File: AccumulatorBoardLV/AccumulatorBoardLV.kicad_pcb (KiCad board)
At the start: 4 copper layers, 152.4 x 50.8 mm, 50 parts, among them J1 Contactor 1, J10 To HV Board, J11 IMD Reset, J12 TS Interlock, J13 Temp Reset, J14 To ECU, J15 Charger LV, J16 Charger Interlock, J17 Lid Interlock, J18 From HV Board, J19 Chip 1, J2 BMS Connector 1, J20 Chip 2, J21 Chip 3, J22 Chip 4, J3 BMS Connector 2, J4 BMS TX, J5 BMS RX, J6 Current Sensor, J7 Contactor 2, J8 IMD LV, J9 BMS Reset, U1 DE1A1B-L2-12V, U10 MCP3008, U11 ISO1050, U12 stm_nucleo_FK303K8, U13 MCP3008, U14 MCP3008, U2 LM555N, U3 SN754410, U4 DE1A1B-L2-12V, U5 L78S05CV-DG, U6 DE1A1B-L2-12V, U7 DK1A1B-12V, U8 ADUM4154ARIZ, U9 MCP3008

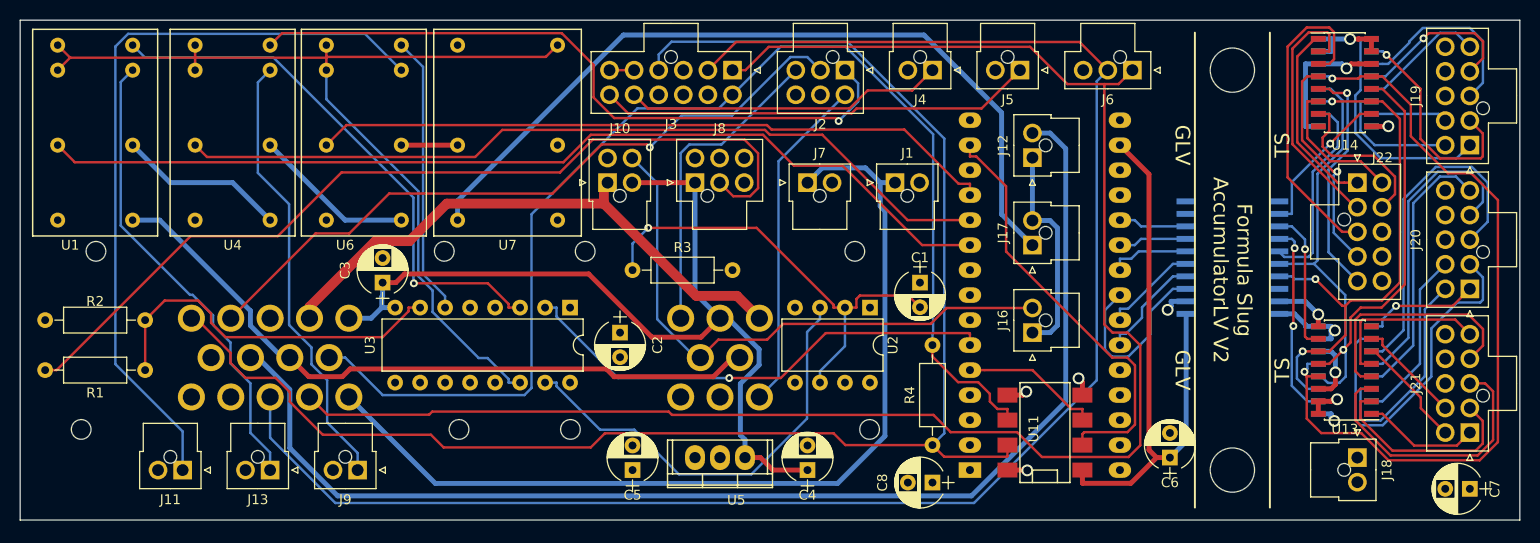
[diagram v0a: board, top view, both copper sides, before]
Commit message: update some footprint throughole sizes
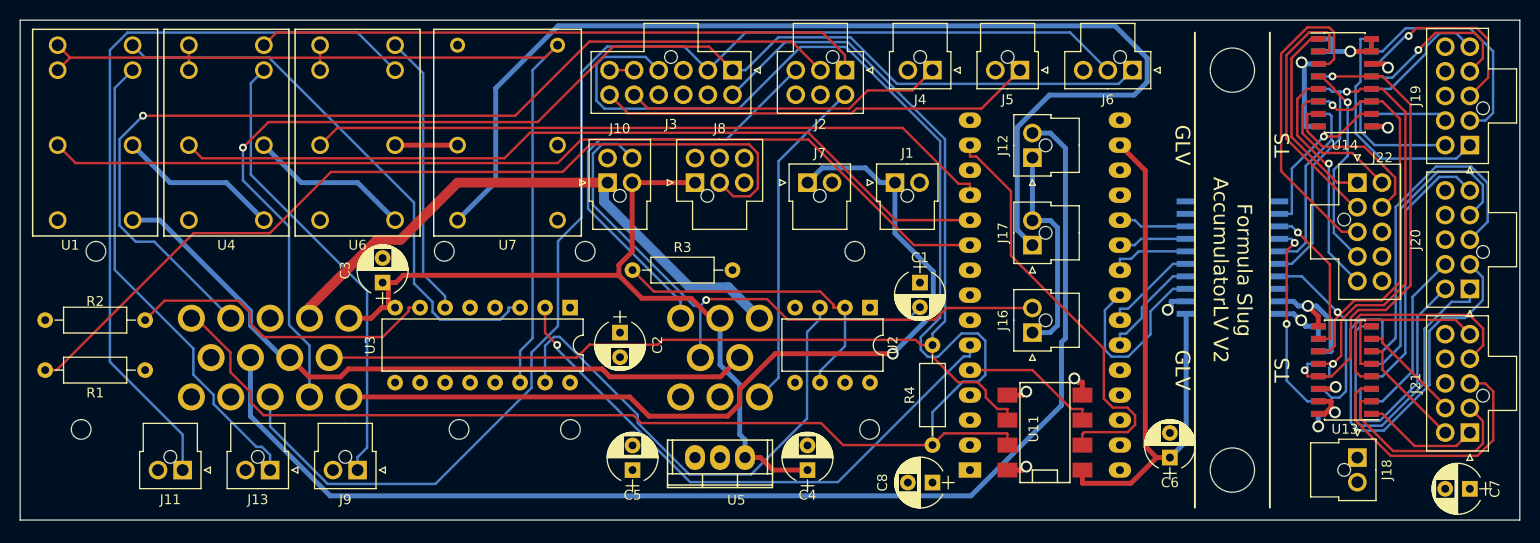
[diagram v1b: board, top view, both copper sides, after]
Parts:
- moved U4 0.63 mm to (57.4, 119.9)
- moved U6 0.63 mm to (70.7, 119.9)
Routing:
- net /5V_BMS: track 170.6 -> 127.7 mm, vias 0 -> 1
- net /SIG_CURRENT: track 171.1 -> 128.9 mm
- net /AIRS_RELAYS_OUT: track 82.3 -> 115.3 mm
- net /SCLK: track 80.1 -> 48.2 mm
- net /CAN_H: track 159.1 -> 188.3 mm
- net /V_L: track 71.7 -> 100.5 mm
- net Net-(J20-Pad1): track 12.0 -> 32.5 mm, vias 1 -> 0
- net /3.3V_TS: track 21.4 -> 35.4 mm
- net /V_S: track 32.0 -> 45.4 mm
- net /TEMP_SSO: track 76.2 -> 65.3 mm, vias 1 -> 2
- net /BATT-: track 31.2 -> 41.6 mm, vias 5 -> 6
- net /TEMP_FLT: track 49.7 -> 58.7 mm
- net +12V: track 91.2 -> 82.5 mm
- net /BMS_FLT: track 70.5 -> 62.1 mm, vias 1 -> 0
- net Net-(J20-Pad2): track 35.1 -> 42.7 mm
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
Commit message: update Arduino (used for STMF3) footprint as well
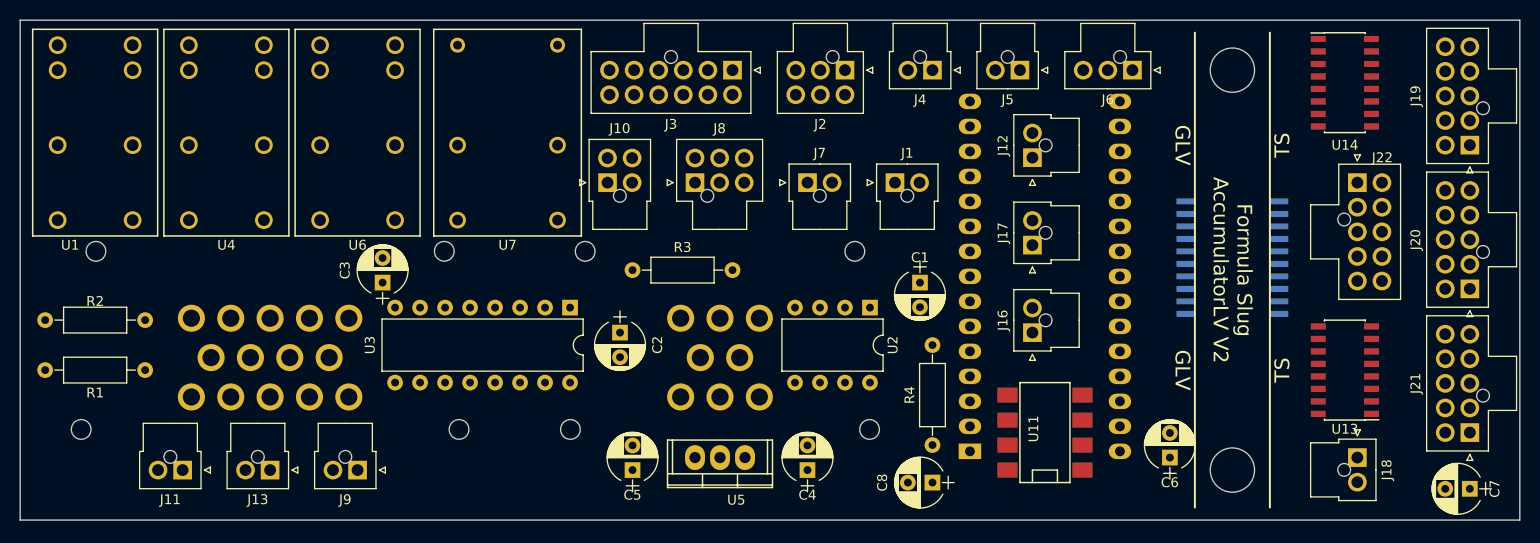
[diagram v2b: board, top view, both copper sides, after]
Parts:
- moved U12 1.91 mm to (144.4, 132.0)
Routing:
- net /CAN_H: track 188.3 -> 0.00 mm
- net /SIG_CURRENT: track 128.9 -> 0.00 mm
- net /5V_BMS: track 127.7 -> 0.00 mm, vias 1 -> 0
- net /AIRS_ACC_OUT: track 125.8 -> 0.00 mm
- net /CAN_L: track 124.2 -> 0.00 mm
- net /AIRS_RELAYS_OUT: track 115.3 -> 0.00 mm
- net /V_L: track 100.5 -> 0.00 mm, vias 1 -> 0
- net /TEMP_FLT_LATCHED: track 98.9 -> 0.00 mm
- net /TIMER_H: track 94.6 -> 0.00 mm
- net /IMD_FLT: track 90.7 -> 0.00 mm
- net /AIRS_FINAL: track 90.4 -> 0.00 mm, vias 1 -> 0
- net /BMS_FLT_LATCHED: track 84.7 -> 0.00 mm
- net +12V: track 82.5 -> 0.00 mm
- net /IMD_RESET: track 77.0 -> 0.00 mm
- net /AIRS_CHARGER_OUT: track 70.6 -> 0.00 mm
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
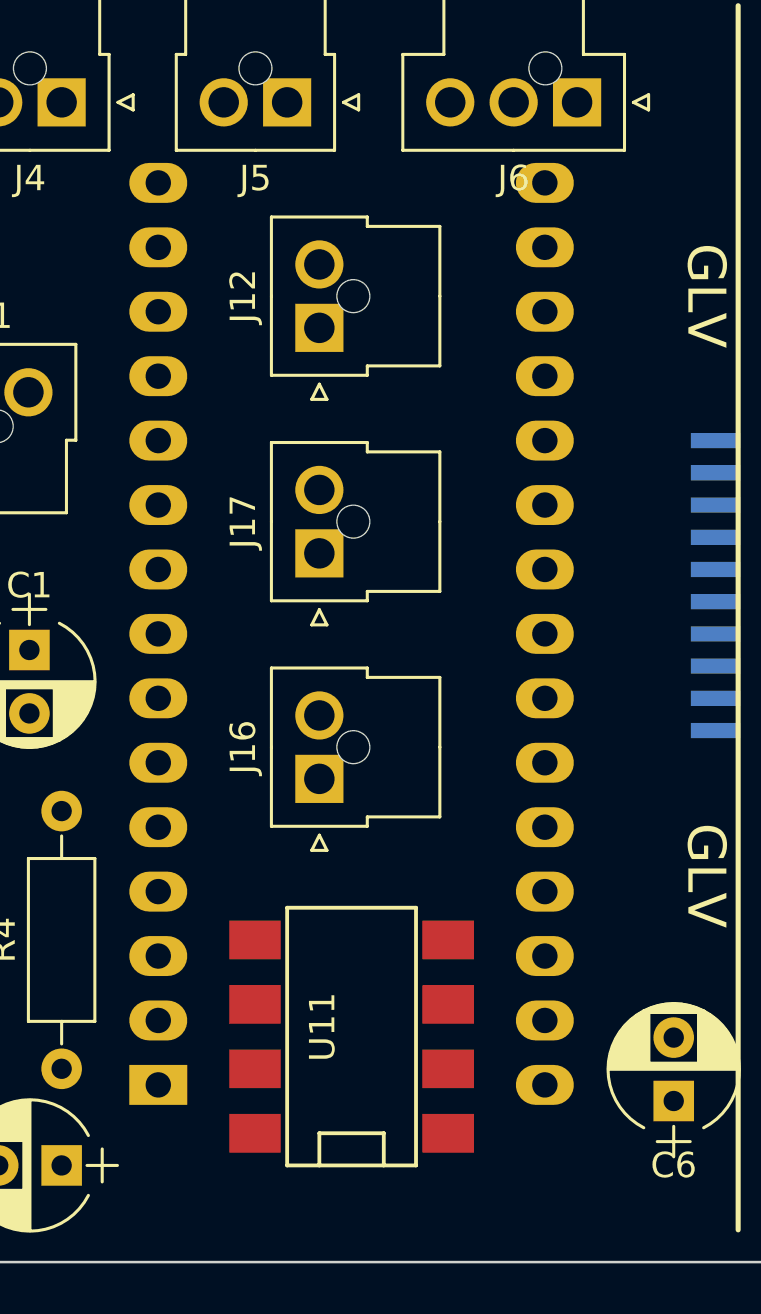
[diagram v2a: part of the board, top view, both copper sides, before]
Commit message: edit PCBs based on actual parts that have arrived
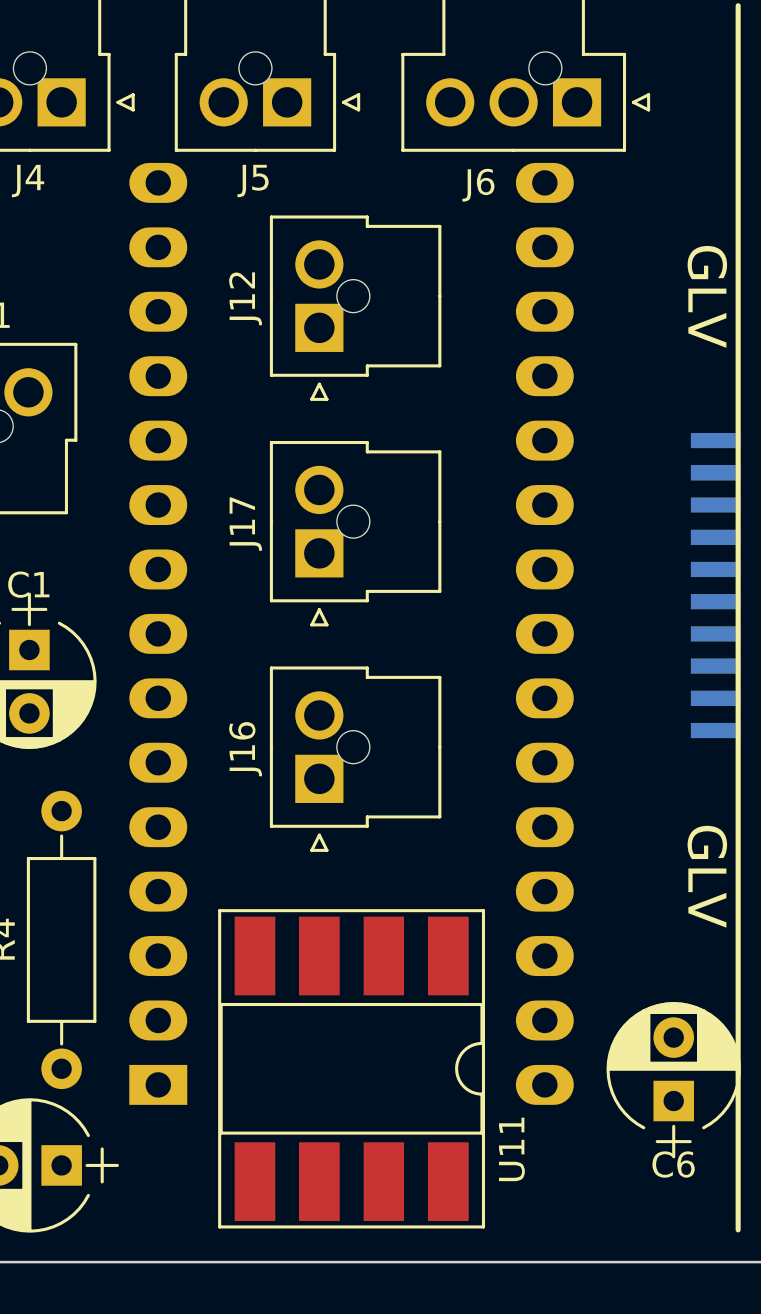
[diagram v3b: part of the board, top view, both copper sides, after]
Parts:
- U11: footprint SMD_Packages:DIP-8_SMD -> Housings_DIP:DIP-8_W8.89mm_SMDSocket_LongPads
- moved U11 1.27 mm to (144.4, 150.4), turned to 270 degrees
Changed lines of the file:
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@@
     (aux_axis_origin 0 0)
     (grid_origin 40.259 157.988)
-    (visible_elements 7FFFFFFF)
+    (visible_elements 7FFFF7FF)
     (pcbplotparams
       (layerselection 0x010fc_80000007)
@@
     (descr "Molex Nano Fit, single row, top entry, through hole, Datasheet:http://www.molex.com/pdm_docs/sd/1053091203_sd.pdf")
     (tags "connector molex nano-fit 105309-xx06")
-    (fp_text reference J6 (at 2.5 -3 180) (layer F.SilkS)
+    (fp_text reference J6 (at 3.81 -3.175 180) (layer F.SilkS)
       (effects (font (size 1 1) (thickness 0.15)))
     )
@@
     )
   )
-  (module SMD_Packages:DIP-8_SMD (layer F.Cu)
-    (at 144.399 149.098 90)
-    (descr "DIP-8_300 smd shape")
-    (tags "smd cms 8dip")
-    (attr smd)
-    (fp_text reference U11 (at 0.381 -1.143 90) (layer F.SilkS)
-      (effects (font (size 1 1) (thickness 0.15)))
-    )
-    (fp_text value ISO1050 (at 0 0.762 90) (layer F.Fab)
-      (effects (font (size 1 1) (thickness 0.15)))
-    )
-    (fp_line (start -5.08 -2.54) (end -5.08 2.54) (layer F.SilkS) (width 0.15))
-    (fp_line (start -5.08 2.54) (end 5.08 2.54) (layer F.SilkS) (width 0.15))
-    (fp_line (start 5.08 2.54) (end 5.08 -2.54) (layer F.SilkS) (width 0.15))
-    (fp_line (start 5.08 -2.54) (end -5.08 -2.54) (layer F.SilkS) (width 0.15))
-    (fp_line (start -5.08 -1.27) (end -3.81 -1.27) (layer F.SilkS) (width 0.15))
-    (fp_line (start -3.81 -1.27) (end -3.81 1.27) (layer F.SilkS) (width 0.15))
-    (fp_line (start -3.81 1.27) (end -5.08 1.27) (layer F.SilkS) (width 0.15))
-    (pad 1 smd rect (at -3.81 3.81 90) (size 1.524 2.032) (layers F.Cu F.Paste F.Mask)
-      (net 5 +3V3))
-    (pad 2 smd rect (at -1.27 3.81 90) (size 1.524 2.032) (layers F.Cu F.Paste F.Mask)
-      (net 77 "Net-(U11-Pad2)"))
-    (pad 3 smd rect (at 1.27 3.81 90) (size 1.524 2.032) (layers F.Cu F.Paste F.Mask)
-      (net 78 "Net-(U11-Pad3)"))
-    (pad 4 smd rect (at 3.81 3.81 90) (size 1.524 2.032) (layers F.Cu F.Paste F.Mask)
-      (net 3 GND))
-    (pad 5 smd rect (at 3.81 -3.81 90) (size 1.524 2.032) (layers F.Cu F.Paste F.Mask)
-      (net 3 GND))
-    (pad 6 smd rect (at 1.27 -3.81 90) (size 1.524 2.032) (layers F.Cu F.Paste F.Mask)
-      (net 16 /CAN_L))
-    (pad 7 smd rect (at -1.27 -3.81 90) (size 1.524 2.032) (layers F.Cu F.Paste F.Mask)
-      (net 14 /CAN_H))
-    (pad 8 smd rect (at -3.81 -3.81 90) (size 1.524 2.032) (layers F.Cu F.Paste F.Mask)
-      (net 1 +5V))
-    (model SMD_Packages.3dshapes/DIP-8_SMD.wrl
-      (at (xyz 0 0 0))
-      (scale (xyz 1 0.5 0.8))
-      (rotate (xyz 0 0 0))
-    )
-  )
   (module Connectors_Molex:Molex_NanoFit_2x05x2.50mm_Straight (layer F.Cu)
     (at 187.579 119.888 90)
@@
       (net 1 +5V))
   )
+  (module Housings_DIP:DIP-8_W8.89mm_SMDSocket_LongPads (layer F.Cu)
+    (at 144.399 150.368 270)
+    (descr "8-lead though-hole mounted DIP package, row spacing 8.89 mm (350 mils), SMDSocket, LongPads")
+    (tags "THT DIP DIL PDIP 2.54mm 8.89mm 350mil SMDSocket LongPads")
+    (attr smd)
+    (fp_text reference U11 (at 3.175 -6.35 270) (layer F.SilkS)
+      (effects (font (size 1 1) (thickness 0.15)))
+    )
+    (fp_text value ISO1050 (at 0 6.14 270) (layer F.Fab)
+      (effects (font (size 1 1) (thickness 0.15)))
+    )
+    (fp_arc (start 0 -5.14) (end -1 -5.14) (angle -180) (layer F.SilkS) (width 0.12))
+    (fp_line (start -2.175 -5.08) (end 3.175 -5.08) (layer F.Fab) (width 0.1))
+    (fp_line (start 3.175 -5.08) (end 3.175 5.08) (layer F.Fab) (width 0.1))
+    (fp_line (start 3.175 5.08) (end -3.175 5.08) (layer F.Fab) (width 0.1))
+    (fp_line (start -3.175 5.08) (end -3.175 -4.08) (layer F.Fab) (width 0.1))
+    (fp_line (start -3.175 -4.08) (end -2.175 -5.08) (layer F.Fab) (width 0.1))
+    (fp_line (start -5.08 -5.14) (end -5.08 5.14) (layer F.Fab) (width 0.1))
+    (fp_line (start -5.08 5.14) (end 5.08 5.14) (layer F.Fab) (width 0.1))
+    (fp_line (start 5.08 5.14) (end 5.08 -5.14) (layer F.Fab) (width 0.1))
+    (fp_line (start 5.08 -5.14) (end -5.08 -5.14) (layer F.Fab) (width 0.1))
+    (fp_line (start -1 -5.14) (end -2.535 -5.14) (layer F.SilkS) (width 0.12))
+    (fp_line (start -2.535 -5.14) (end -2.535 5.14) (layer F.SilkS) (width 0.12))
+    (fp_line (start -2.535 5.14) (end 2.535 5.14) (layer F.SilkS) (width 0.12))
+    (fp_line (start 2.535 5.14) (end 2.535 -5.14) (layer F.SilkS) (width 0.12))
+    (fp_line (start 2.535 -5.14) (end 1 -5.14) (layer F.SilkS) (width 0.12))
+    (fp_line (start -6.235 -5.2) (end -6.235 5.2) (layer F.SilkS) (width 0.12))
+    (fp_line (start -6.235 5.2) (end 6.235 5.2) (layer F.SilkS) (width 0.12))
+    (fp_line (start 6.235 5.2) (end 6.235 -5.2) (layer F.SilkS) (width 0.12))
+    (fp_line (start 6.235 -5.2) (end -6.235 -5.2) (layer F.SilkS) (width 0.12))
+    (fp_line (start -6.25 -5.4) (end -6.25 5.4) (layer F.CrtYd) (width 0.05))
+    (fp_line (start -6.25 5.4) (end 6.25 5.4) (layer F.CrtYd) (width 0.05))
+    (fp_line (start 6.25 5.4) (end 6.25 -5.4) (layer F.CrtYd) (width 0.05))
+    (fp_line (start 6.25 -5.4) (end -6.25 -5.4) (layer F.CrtYd) (width 0.05))
+    (fp_text user %R (at 0 0 270) (layer F.Fab)
+      (effects (font (size 1 1) (thickness 0.15)))
+    )
+    (pad 1 smd rect (at -4.445 -3.81 270) (size 3.1 1.6) (layers F.Cu F.Paste F.Mask)
+      (net 5 +3V3))
+    (pad 5 smd rect (at 4.445 3.81 270) (size 3.1 1.6) (layers F.Cu F.Paste F.Mask)
+      (net 3 GND))
+    (pad 2 smd rect (at -4.445 -1.27 270) (size 3.1 1.6) (layers F.Cu F.Paste F.Mask)
+      (net 77 "Net-(U11-Pad2)"))
+    (pad 6 smd rect (at 4.445 1.27 270) (size 3.1 1.6) (layers F.Cu F.Paste F.Mask)
+      (net 16 /CAN_L))
+    (pad 3 smd rect (at -4.445 1.27 270) (size 3.1 1.6) (layers F.Cu F.Paste F.Mask)
+      (net 78 "Net-(U11-Pad3)"))
+    (pad 7 smd rect (at 4.445 -1.27 270) (size 3.1 1.6) (layers F.Cu F.Paste F.Mask)
+      (net 14 /CAN_H))
+    (pad 4 smd rect (at -4.445 3.81 270) (size 3.1 1.6) (layers F.Cu F.Paste F.Mask)
+      (net 3 GND))
+    (pad 8 smd rect (at 4.445 -3.81 270) (size 3.1 1.6) (layers F.Cu F.Paste F.Mask)
+      (net 1 +5V))
+    (model ${KISYS3DMOD}/Housings_DIP.3dshapes/DIP-8_W8.89mm_SMDSocket.wrl
+      (at (xyz 0 0 0))
+      (scale (xyz 1 1 1))
+      (rotate (xyz 0 0 0))
+    )
+  )
   (gr_text GLV (at 158.369 119.888 270) (layer B.SilkS)

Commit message: prepare to re-send PE LV board
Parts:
- moved C7 22.9 mm to (170.4, 139.6), turned to 270 degrees
- moved C8 22.2 mm to (155.2, 154.8), turned to 0 degrees
- moved J18 13.3 mm to (176.1, 138.3), turned to 0 degrees
- moved C6 9.09 mm to (155.2, 142.7), turned to 0 degrees
- moved U10 8.89 mm to (174.9, 151.6)
- moved U13 8.89 mm to (174.9, 151.6)
- moved J21 5.08 mm to (187.6, 154.2)
- moved J20 3.18 mm to (187.6, 137.7)
- moved J19 1.27 mm to (187.6, 121.2)
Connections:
- net Net-(U11-Pad2) renamed /CAN_RX
- net Net-(U11-Pad3) renamed /CAN_TX
- U12 pad 30: +5V -> +12V
- U8 pad 10: (no net) -> GND
- U8 pad 11: (no net) -> /BATT-
- U8 pad 18: (no net) -> /SCLK
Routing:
- net /5V_BMS: track 0.00 -> 168.4 mm
- net /TIMER_H: track 0.00 -> 147.7 mm
- net /CAN_H: track 0.00 -> 146.8 mm
- net /CAN_L: track 0.00 -> 141.6 mm
- net +12V: track 0.00 -> 114.4 mm
- net /SIG_CURRENT: track 0.00 -> 105.2 mm, vias 0 -> 1
- net /AIRS_ACC_OUT: track 0.00 -> 103.7 mm, vias 0 -> 1
- net /TEMP_FLT_LATCHED: track 0.00 -> 98.1 mm
- net /IMD_FLT_H: track 0.00 -> 96.1 mm
- net /TEMP_FLT_H: track 0.00 -> 91.8 mm
- net /IMD_FLT: track 0.00 -> 90.5 mm
- net /BMS_FLT_LATCHED: track 0.00 -> 84.4 mm
- net /IMD_RESET: track 0.00 -> 83.4 mm
- net /SCLK: track 0.00 -> 81.8 mm, vias 0 -> 2
- net /AIRS_RELAYS_OUT: track 0.00 -> 78.1 mm, vias 0 -> 2
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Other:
- net class Ground removed
- net class Power: trace_width 1 -> 1.25

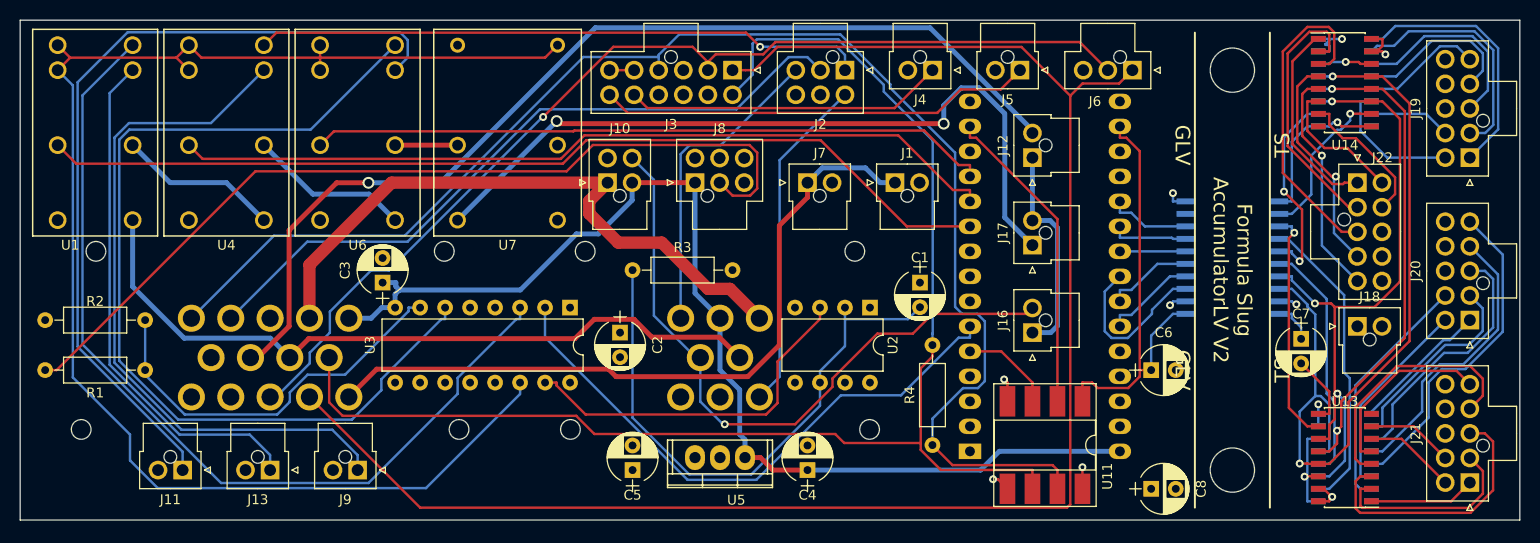
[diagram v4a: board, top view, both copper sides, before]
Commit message: fix AccumulatorLV board based on real life testing
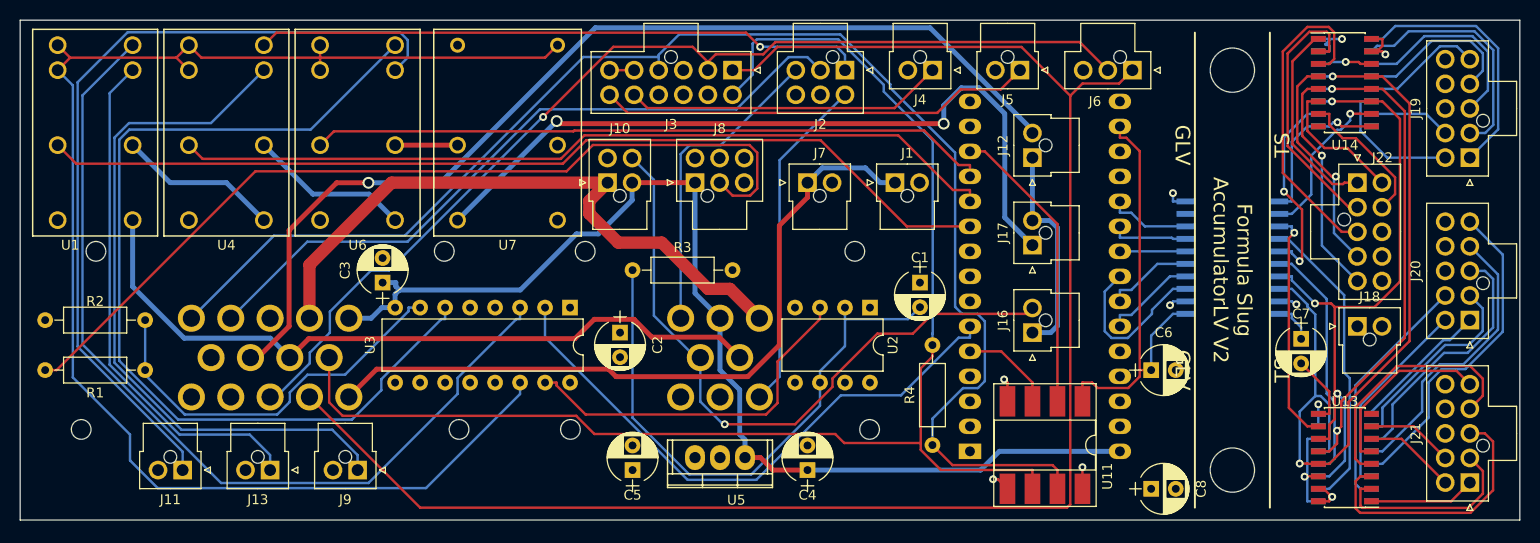
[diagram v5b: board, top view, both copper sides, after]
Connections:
- U12 pad 13: (no net) -> /CAN_RX
- U12 pad 14: /CAN_RX -> (no net)
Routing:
- net /CAN_RX: track 32.0 -> 30.0 mm
